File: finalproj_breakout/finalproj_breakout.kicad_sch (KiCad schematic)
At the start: 29 parts, among them J1 Conn_02x18_Odd_Even, J2 Conn_02x18_Odd_Even, J3 Conn_02x18_Odd_Even, J4 Conn_02x18_Odd_Even, J8 Programmer_Conn, SW1 RESET_SW, U1 STM32F767ZITx

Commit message: B-B-BREAAKKOUTTTgit add finalproj_breakout
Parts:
- C10, C11, C12, C13, C14, C15, C16, C17, C18, C19, C20, C21, C22, C3, C4, C5, C6, C7, C8, C9: footprint (none) -> Capacitor_SMD:C_1812_4532Metric_Pad1.57x3.40mm_HandSolder
- C23: value C -> 0.1uF; footprint (none) -> Capacitor_SMD:C_1812_4532Metric_Pad1.57x3.40mm_HandSolder
- R1: footprint Resistor_SMD:R_1020_2550Metric_Pad1.33x5.20mm_HandSolder -> Resistor_SMD:R_2816_7142Metric_Pad3.20x4.45mm_HandSolder
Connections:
- net PDR_)N is gone; now on net PDR_ON: U1.143 (PDR_ON)
- net Pb4 is gone; now on net PB4: U1.134 (PB4)
- net SWCLK is gone; now on net PA14: J8.2 (SWCLK)
- net SWDIO is gone; now on net PA13: J8.4 (SWDIO)
- net VSSA is gone; now on net GND: J2.31 (Pin_31), U1.31 (VSSA)
- net pF11 is gone; now on net PF11: U1.49 (PF11)
- net GND: no longer J1.30 (Pin_30), R1.2
- new net BOOT0: J1.30 (Pin_30), R1.2

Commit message: finished a quarter of breakout board connections, placed cap on the back
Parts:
- J1, J2, J3, J4: footprint Connector_PinHeader_2.54mm:PinHeader_2x18_P2.54mm_Vertical_SMD -> Connector_PinHeader_2.54mm:PinHeader_2x18_P2.54mm_Vertical
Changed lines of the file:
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@@
       (effects (font (size 1.27 1.27)))
     )
-    (property "Footprint" "Connector_PinHeader_2.54mm:PinHeader_2x18_P2.54mm_Vertical_SMD" (at 240.03 169.545 0)
+    (property "Footprint" "Connector_PinHeader_2.54mm:PinHeader_2x18_P2.54mm_Vertical" (at 240.03 169.545 0)
       (effects (font (size 1.27 1.27)) hide)
     )
@@
       (effects (font (size 1.27 1.27)) (justify left))
     )
-    (property "Footprint" "Connector_PinHeader_2.54mm:PinHeader_2x18_P2.54mm_Vertical_SMD" (at 275.59 207.645 0)
+    (property "Footprint" "Connector_PinHeader_2.54mm:PinHeader_2x18_P2.54mm_Vertical" (at 275.59 207.645 0)
       (effects (font (size 1.27 1.27)) hide)
     )
@@
       (effects (font (size 1.27 1.27)) (justify left))
     )
-    (property "Footprint" "Connector_PinHeader_2.54mm:PinHeader_2x18_P2.54mm_Vertical_SMD" (at 275.59 135.255 0)
+    (property "Footprint" "Connector_PinHeader_2.54mm:PinHeader_2x18_P2.54mm_Vertical" (at 275.59 135.255 0)
       (effects (font (size 1.27 1.27)) hide)
     )
@@
       (effects (font (size 1.27 1.27)))
     )
-    (property "Footprint" "Connector_PinHeader_2.54mm:PinHeader_2x18_P2.54mm_Vertical_SMD" (at 313.69 170.18 0)
-      (effects (font (size 1.27 1.27)) hide)
-    )
+    (property "Footprint" "Connector_PinHeader_2.54mm:PinHeader_2x18_P2.54mm_Vertical" (at 313.69 170.18 0)
+      (effects (font (size 1.27 1.27)) hide)
+    )

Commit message: Removed unused files (breakoutalt), fixed alignment issue of header pins
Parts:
- J1, J2, J3, J4: footprint Connector_PinHeader_2.54mm:PinHeader_2x18_P2.54mm_Vertical -> Connector_PinHeader_2.54mm:PinHeader_2x18_P2.54mm_Vertical_DoubleSided
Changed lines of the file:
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@@
       (effects (font (size 1.27 1.27)))
     )
-    (property "Footprint" "Connector_PinHeader_2.54mm:PinHeader_2x18_P2.54mm_Vertical" (at 240.03 169.545 0)
+    (property "Footprint" "Connector_PinHeader_2.54mm:PinHeader_2x18_P2.54mm_Vertical_DoubleSided" (at 240.03 169.545 0)
       (effects (font (size 1.27 1.27)) hide)
     )
@@
       (effects (font (size 1.27 1.27)) (justify left))
     )
-    (property "Footprint" "Connector_PinHeader_2.54mm:PinHeader_2x18_P2.54mm_Vertical" (at 275.59 207.645 0)
+    (property "Footprint" "Connector_PinHeader_2.54mm:PinHeader_2x18_P2.54mm_Vertical_DoubleSided" (at 275.59 207.645 0)
       (effects (font (size 1.27 1.27)) hide)
     )
@@
       (effects (font (size 1.27 1.27)) (justify left))
     )
-    (property "Footprint" "Connector_PinHeader_2.54mm:PinHeader_2x18_P2.54mm_Vertical" (at 275.59 135.255 0)
+    (property "Footprint" "Connector_PinHeader_2.54mm:PinHeader_2x18_P2.54mm_Vertical_DoubleSided" (at 275.59 135.255 0)
       (effects (font (size 1.27 1.27)) hide)
     )
@@
       (effects (font (size 1.27 1.27)))
     )
-    (property "Footprint" "Connector_PinHeader_2.54mm:PinHeader_2x18_P2.54mm_Vertical" (at 313.69 170.18 0)
-      (effects (font (size 1.27 1.27)) hide)
-    )
+    (property "Footprint" "Connector_PinHeader_2.54mm:PinHeader_2x18_P2.54mm_Vertical_DoubleSided" (at 313.69 170.18 0)
+      (effects (font (size 1.27 1.27)) hide)
+    )

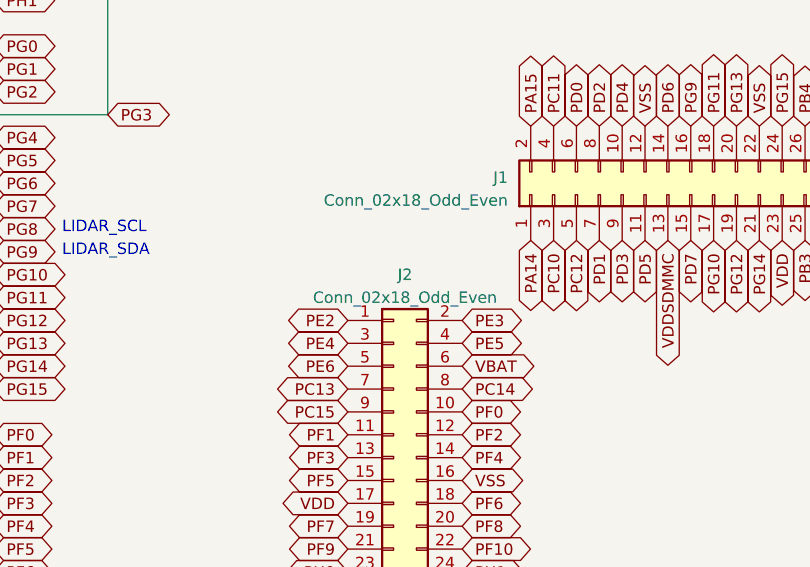
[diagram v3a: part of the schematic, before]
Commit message: fixed DRC erros on main board, had to revert breakout board headers to one sided since couldn't find lib
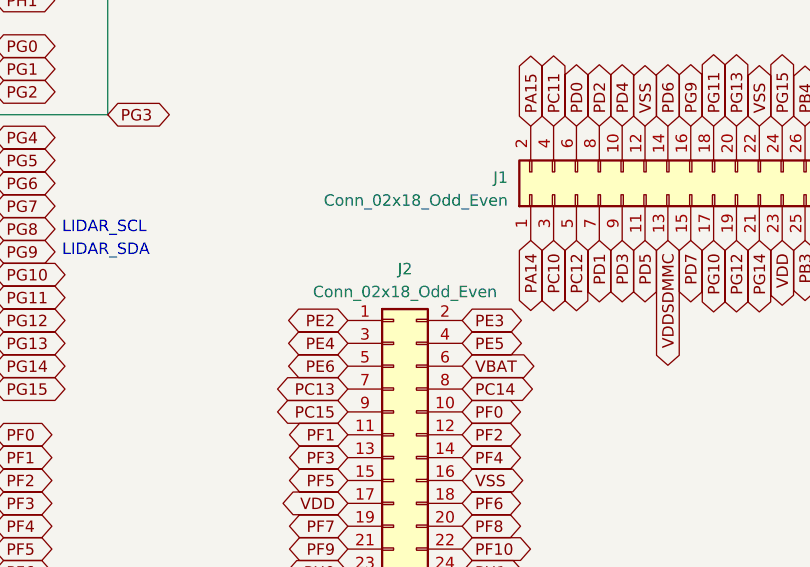
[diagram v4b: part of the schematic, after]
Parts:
- J1, J2, J3, J4: footprint Connector_PinHeader_2.54mm:PinHeader_2x18_P2.54mm_Vertical_DoubleSided -> Connector_PinHeader_2.54mm:PinHeader_2x18_P2.54mm_Vertical
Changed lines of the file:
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@@
   (symbol (lib_id "Connector_Generic:Conn_02x18_Odd_Even") (at 240.03 169.545 0) (unit 1)
     (in_bom yes) (on_board yes) (dnp no) (fields_autoplaced)
-    (property "Reference" "J2" (at 241.3 144.145 0)
-      (effects (font (size 1.27 1.27)))
-    )
-    (property "Value" "Conn_02x18_Odd_Even" (at 241.3 146.685 0)
-      (effects (font (size 1.27 1.27)))
-    )
-    (property "Footprint" "Connector_PinHeader_2.54mm:PinHeader_2x18_P2.54mm_Vertical_DoubleSided" (at 240.03 169.545 0)
+    (property "Reference" "J2" (at 241.3 143.51 0)
+      (effects (font (size 1.27 1.27)))
+    )
+    (property "Value" "Conn_02x18_Odd_Even" (at 241.3 146.05 0)
+      (effects (font (size 1.27 1.27)))
+    )
+    (property "Footprint" "Connector_PinHeader_2.54mm:PinHeader_2x18_P2.54mm_Vertical" (at 240.03 169.545 0)
       (effects (font (size 1.27 1.27)) hide)
     )
@@
       (effects (font (size 1.27 1.27)) (justify left))
     )
-    (property "Footprint" "Connector_PinHeader_2.54mm:PinHeader_2x18_P2.54mm_Vertical_DoubleSided" (at 275.59 207.645 0)
+    (property "Footprint" "Connector_PinHeader_2.54mm:PinHeader_2x18_P2.54mm_Vertical" (at 275.59 207.645 0)
       (effects (font (size 1.27 1.27)) hide)
     )
@@
       (effects (font (size 1.27 1.27)) (justify left))
     )
-    (property "Footprint" "Connector_PinHeader_2.54mm:PinHeader_2x18_P2.54mm_Vertical_DoubleSided" (at 275.59 135.255 0)
+    (property "Footprint" "Connector_PinHeader_2.54mm:PinHeader_2x18_P2.54mm_Vertical" (at 275.59 135.255 0)
       (effects (font (size 1.27 1.27)) hide)
     )
@@
       (effects (font (size 1.27 1.27)))
     )
-    (property "Footprint" "Connector_PinHeader_2.54mm:PinHeader_2x18_P2.54mm_Vertical_DoubleSided" (at 313.69 170.18 0)
-      (effects (font (size 1.27 1.27)) hide)
-    )
+    (property "Footprint" "Connector_PinHeader_2.54mm:PinHeader_2x18_P2.54mm_Vertical" (at 313.69 170.18 0)
+      (effects (font (size 1.27 1.27)) hide)
+    )

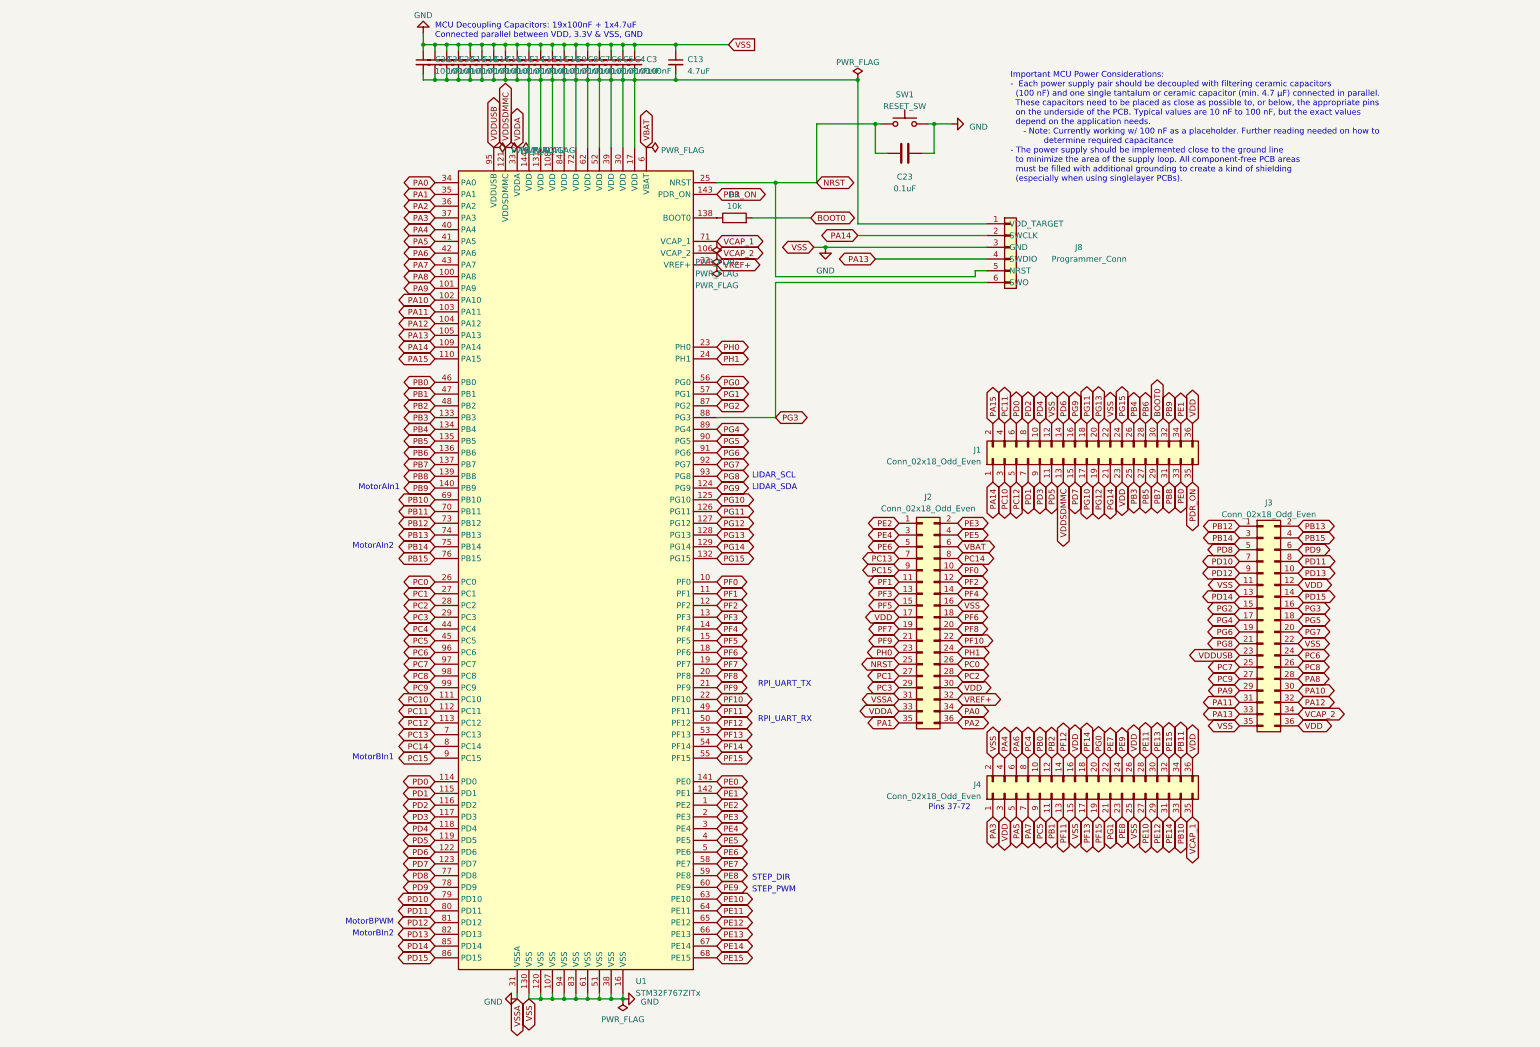
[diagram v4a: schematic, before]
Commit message: Added necessary pin requirements to mainboard
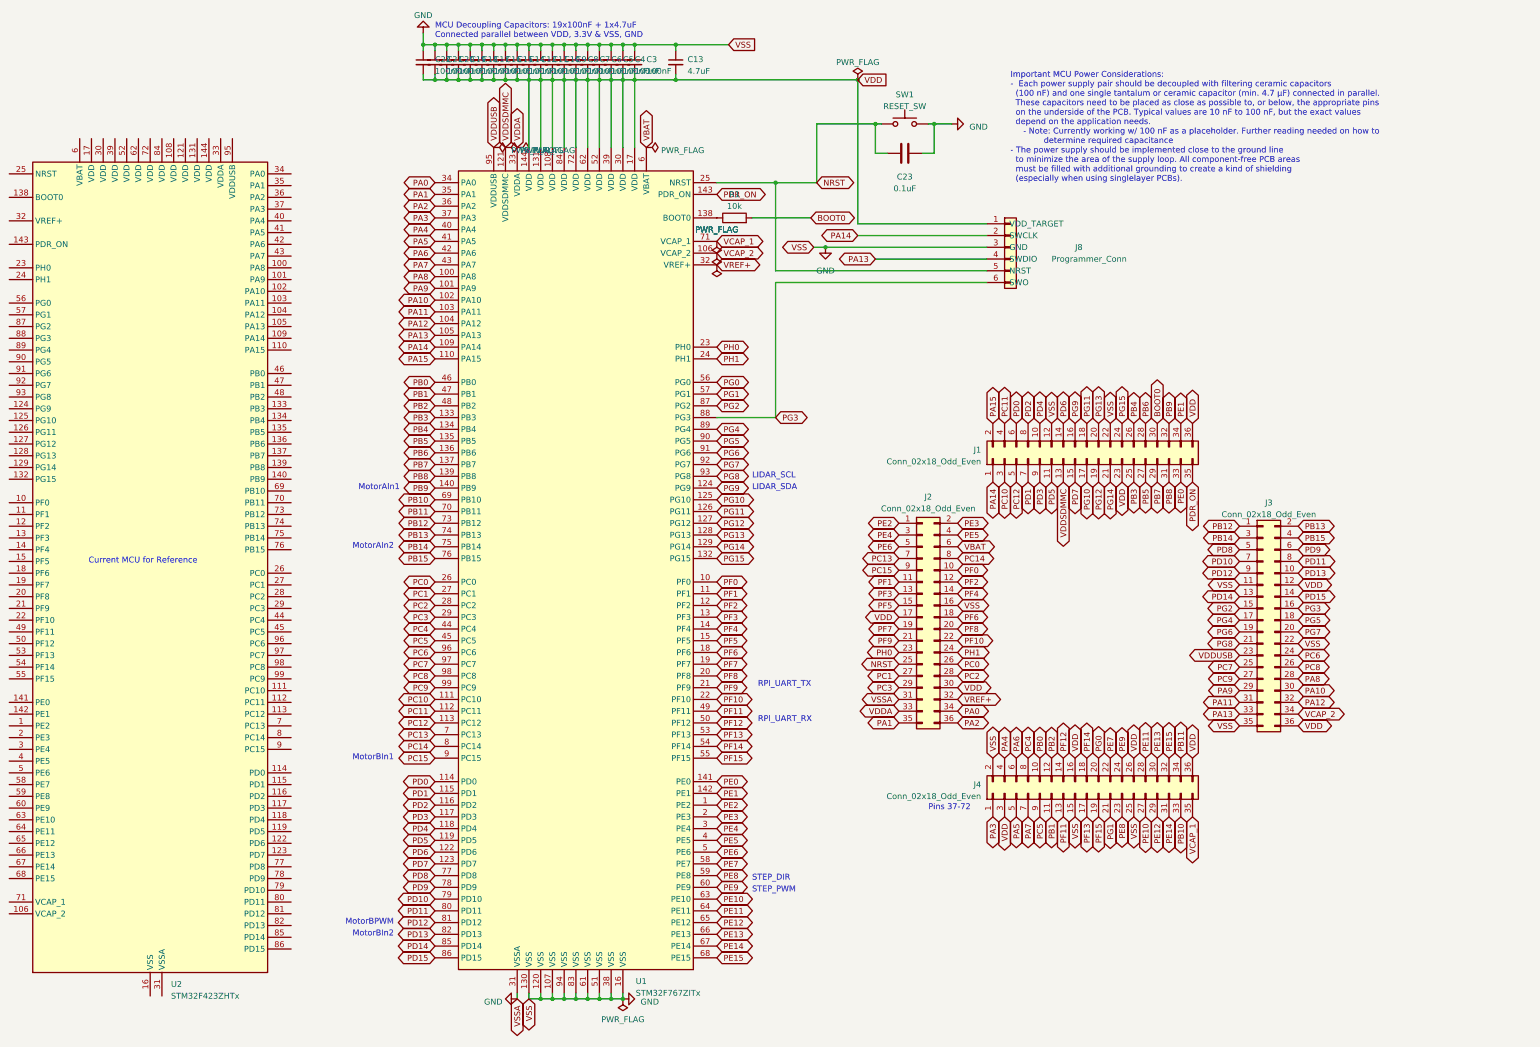
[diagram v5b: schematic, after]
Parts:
- added U2: STM32F423ZHTx, Package_QFP:LQFP-144_20x20mm_P0.5mm, symbol MCU_ST_STM32F4:STM32F423ZHTx
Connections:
- net VDD: now also C10.2, C11.2, C12.2, C13.2, C14.2, C15.2, C16.2, C17.2, C18.2, C19.2, C20.2, C21.2, C22.2, C3.2, C4.2, C5.2, C6.2, C7.2, C8.2, C9.2, J8.1 (VDD_TARGET), U1.108 (VDD), U1.131 (VDD), U1.144 (VDD), U1.17 (VDD), U1.30 (VDD), U1.39 (VDD), U1.52 (VDD), U1.62 (VDD), U1.72 (VDD), U1.84 (VDD)
- new net: U2.107 (VSS), U2.120 (VSS), U2.130 (VSS), U2.16 (VSS), U2.38 (VSS), U2.51 (VSS), U2.61 (VSS), U2.83 (VSS), U2.94 (VSS)
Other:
- note added: "Current MCU for Reference"
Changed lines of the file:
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@@
   (junction (at 149.86 53.34) (diameter 0) (color 0 0 0 0)
   )
-  (wire (pts (xy 208.28 95.885) (xy 208.28 75.565))
+  (wire (pts (xy 208.28 94.615) (xy 208.28 75.565))
     (stroke (width 0) (type default))
   )
@@
     (stroke (width 0) (type default))
   )
-  (wire (pts (xy 251.46 95.885) (xy 251.46 94.615))
-    (stroke (width 0) (type default))
-  )
   (wire (pts (xy 229.87 92.075) (xy 254 92.075))
     (stroke (width 0) (type default))
@@
     (stroke (width 0) (type default))
   )
-  (wire (pts (xy 208.28 95.885) (xy 251.46 95.885))
-    (stroke (width 0) (type default))
-  )
   (wire (pts (xy 139.7 45.72) (xy 142.24 45.72))
     (stroke (width 0) (type default))
@@
     (stroke (width 0) (type default))
   )
-  (wire (pts (xy 251.46 94.615) (xy 254 94.615))
+  (wire (pts (xy 208.28 94.615) (xy 254 94.615))
     (stroke (width 0) (type default))
   )
@@
   (text "MotorBIn1" (at 125.73 200.66 0)
     (effects (font (size 1.27 1.27)) (justify right bottom))
+  )
+  (text "Current MCU for Reference" (at 59.69 158.115 0)
+    (effects (font (size 1.27 1.27)) (justify left bottom))
   )
   (text "MotorBIn2" (at 125.73 238.76 0)
@@
     (property "Intersheetrefs" "${INTERSHEET_REFS}" (at 125.8253 111.125 0)
       (effects (font (size 1.27 1.27)) (justify right) hide)
+    )
+  )
+  (global_label "VDD" (shape input) (at 226.06 53.34 0) (fields_autoplaced)
+    (effects (font (size 1.27 1.27)) (justify left))
+    (property "Intersheetrefs" "${INTERSHEET_REFS}" (at 232.5944 53.34 0)
+      (effects (font (size 1.27 1.27)) (justify left) hide)
     )
   )
@@
   )
   (symbol (lib_id "power:PWR_FLAG") (at 195.58 93.345 180) (unit 1)
-    (in_bom yes) (on_board yes) (dnp no) (fields_autoplaced)
+    (in_bom yes) (on_board yes) (dnp no)
     (property "Reference" "#FLG01" (at 195.58 95.25 0)
       (effects (font (size 1.27 1.27)) hide)
     )
-    (property "Value" "PWR_FLAG" (at 195.58 97.79 0)
+    (property "Value" "PWR_FLAG" (at 195.58 85.725 0)
       (effects (font (size 1.27 1.27)))
     )
@@
   )
   (symbol (lib_id "power:PWR_FLAG") (at 195.58 90.805 180) (unit 1)
-    (in_bom yes) (on_board yes) (dnp no) (fields_autoplaced)
+    (in_bom yes) (on_board yes) (dnp no)
     (property "Reference" "#FLG03" (at 195.58 92.71 0)
       (effects (font (size 1.27 1.27)) hide)
     )
-    (property "Value" "PWR_FLAG" (at 195.58 95.25 0)
+    (property "Value" "PWR_FLAG" (at 195.58 85.725 0)
       (effects (font (size 1.27 1.27)))
     )
@@
   )
   (symbol (lib_id "power:PWR_FLAG") (at 195.58 88.265 180) (unit 1)
-    (in_bom yes) (on_board yes) (dnp no) (fields_autoplaced)
+    (in_bom yes) (on_board yes) (dnp no)
     (property "Reference" "#FLG04" (at 195.58 90.17 0)
       (effects (font (size 1.27 1.27)) hide)
     )
-    (property "Value" "PWR_FLAG" (at 195.58 92.71 0)
+    (property "Value" "PWR_FLAG" (at 195.58 85.725 0)
       (effects (font (size 1.27 1.27)))
     )
@@
         )
       )
+    )
+  )
+  (symbol (lib_id "MCU_ST_STM32F4:STM32F423ZHTx") (at 73.025 160.02 0) (unit 1)
+    (in_bom yes) (on_board yes) (dnp no) (fields_autoplaced)
+    (property "Reference" "U2" (at 77.5209 248.92 0)
+      (effects (font (size 1.27 1.27)) (justify left))
+    )
+    (property "Value" "STM32F423ZHTx" (at 77.5209 251.46 0)
+      (effects (font (size 1.27 1.27)) (justify left))
+    )
+    (property "Footprint" "Package_QFP:LQFP-144_20x20mm_P0.5mm" (at 47.625 246.38 0)
+      (effects (font (size 1.27 1.27)) (justify right) hide)
+    )
+    (property "Datasheet" "https://www.st.com/resource/en/datasheet/stm32f423zh.pdf" (at 73.025 160.02 0)
+      (effects (font (size 1.27 1.27)) hide)
+    )
+    (pin "1")
+    (pin "10")
+    (pin "100")
+    (pin "101")
+    (pin "102")
+    (pin "103")
+    (pin "104")
+    (pin "105")
+    (pin "106")
+    (pin "107")
+    (pin "108")
+    (pin "109")
+    (pin "11")
+    (pin "110")
+    (pin "111")
+    (pin "112")
+    (pin "113")
+    (pin "114")
+    (pin "115")
+    (pin "116")
+    (pin "117")
+    (pin "118")
+    (pin "119")
+    (pin "12")
+    (pin "120")
+    (pin "121")
+    (pin "122")
+    (pin "123")
+    (pin "124")
+    (pin "125")
+    (pin "126")
+    (pin "127")
+    (pin "128")
+    (pin "129")
+    (pin "13")
+    (pin "130")
+    (pin "131")
+    (pin "132")
+    (pin "133")
+    (pin "134")
+    (pin "135")
+    (pin "136")
+    (pin "137")
+    (pin "138")
+    (pin "139")
+    (pin "14")
+    (pin "140")
+    (pin "141")
+    (pin "142")
+    (pin "143")
+    (pin "144")
+    (pin "15")
+    (pin "16")
+    (pin "17")
+    (pin "18")
+    (pin "19")
+    (pin "2")
+    (pin "20")
+    (pin "21")
+    (pin "22")
+    (pin "23")
+    (pin "24")
+    (pin "25")
+    (pin "26")
+    (pin "27")
+    (pin "28")
+    (pin "29")
+    (pin "3")
+    (pin "30")
+    (pin "31")
+    (pin "32")
+    (pin "33")
+    (pin "34")
+    (pin "35")
+    (pin "36")
+    (pin "37")
+    (pin "38")
+    (pin "39")
+    (pin "4")
+    (pin "40")
+    (pin "41")
+    (pin "42")
+    (pin "43")
+    (pin "44")
+    (pin "45")
+    (pin "46")
+    (pin "47")
+    (pin "48")
+    (pin "49")
+    (pin "5")
+    (pin "50")
+    (pin "51")
+    (pin "52")
+    (pin "53")
+    (pin "54")
+    (pin "55")
+    (pin "56")
+    (pin "57")
+    (pin "58")
+    (pin "59")
+    (pin "6")
+    (pin "60")
+    (pin "61")
+    (pin "62")
+    (pin "63")
+    (pin "64")
+    (pin "65")
+    (pin "66")
+    (pin "67")
+    (pin "68")
+    (pin "69")
+    (pin "7")
+    (pin "70")
+    (pin "71")
+    (pin "72")
+    (pin "73")
+    (pin "74")
+    (pin "75")
+    (pin "76")
+    (pin "77")
+    (pin "78")
+    (pin "79")
+    (pin "8")
+    (pin "80")
+    (pin "81")
+    (pin "82")
+    (pin "83")
+    (pin "84")
+    (pin "85")
+    (pin "86")
+    (pin "87")
+    (pin "88")
+    (pin "89")
+    (pin "9")
+    (pin "90")
+    (pin "91")
+    (pin "92")
+    (pin "93")
+    (pin "94")
+    (pin "95")
+    (pin "96")
+    (pin "97")
+    (pin "98")
+    (pin "99")
+    (instances
+      (project "finalproj_breakout"
+        (path "/08d1c057-d836-4496-aa4e-f556547e7c14"
+          (reference "U2") (unit 1)
+        )
+      )
